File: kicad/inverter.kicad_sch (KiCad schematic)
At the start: 3 parts, among them Q2 2N3904

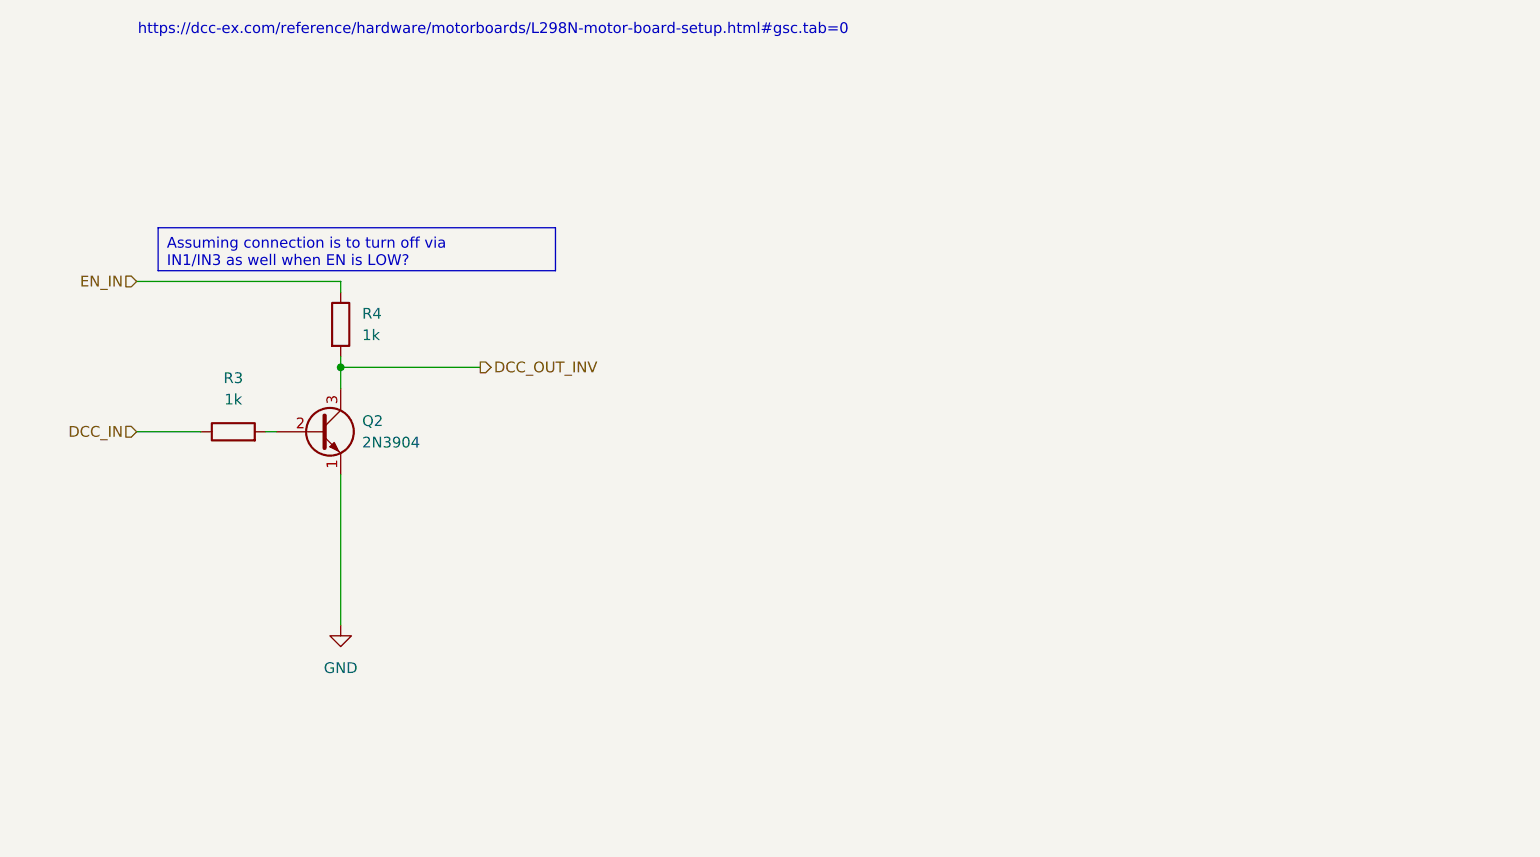
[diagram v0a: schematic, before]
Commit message: new screen, minimum functional
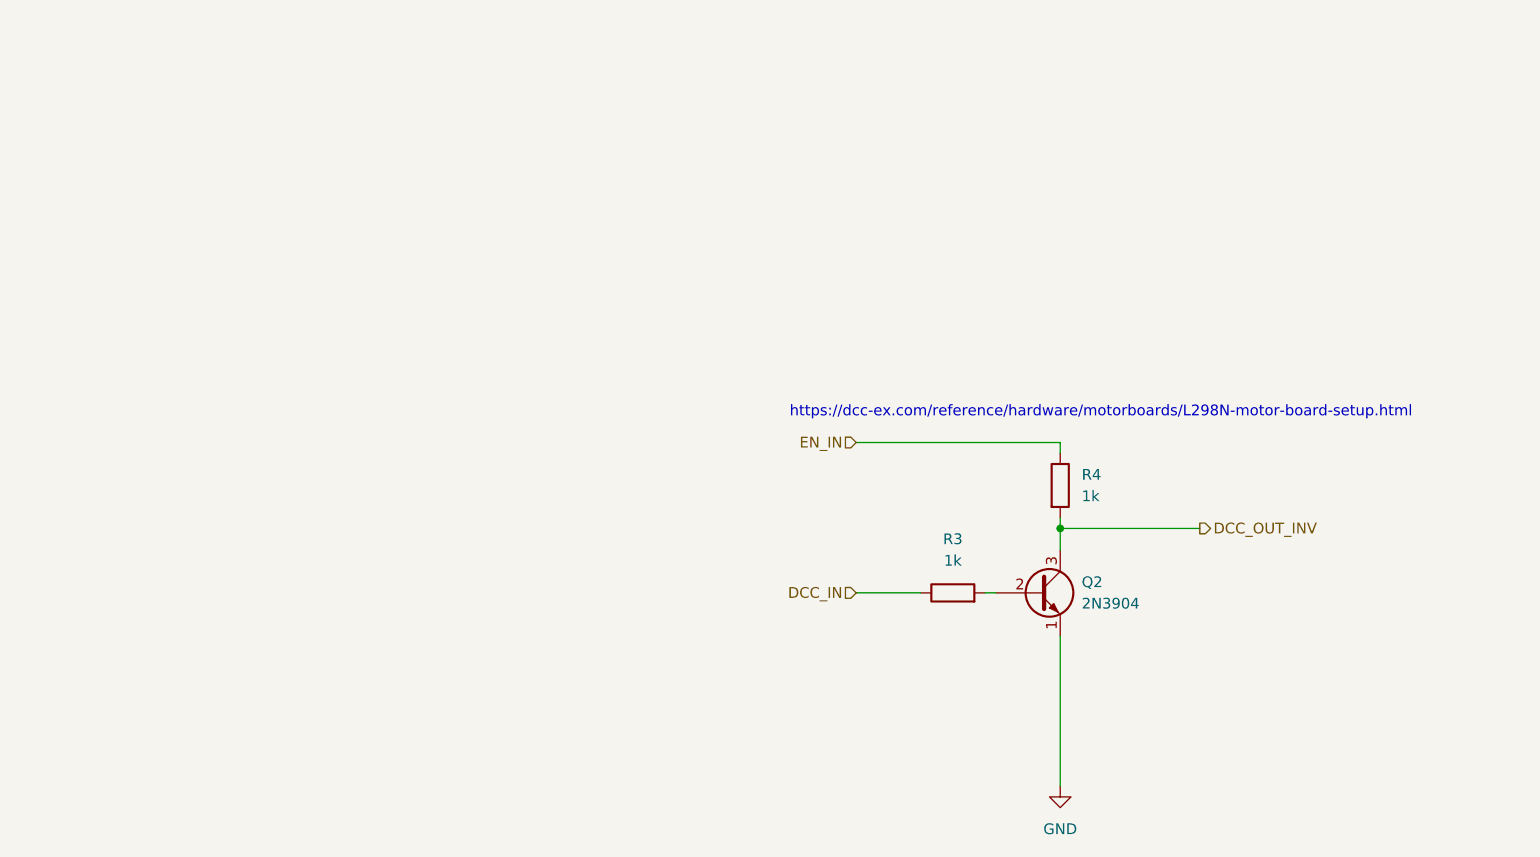
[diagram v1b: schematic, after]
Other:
- note added: "https://dcc-ex.com/reference/hardware/motorboards/L298N-motor-board-setup.html"
- note removed: "https://dcc-ex.com/reference/hardware/motorboards/L298N-motor-board-setup.html#gsc.tab=0"
- moved on the sheet: Q2, R3, R4
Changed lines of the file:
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@@
 	(paper "A4")
 	(junction
-		(at 55.88 85.09)
+		(at 140.97 104.14)
 		(diameter 0)
 		(color 0 0 0 0)
@@
 	(wire
 		(pts
-			(xy 55.88 85.09) (xy 55.88 87.63)
-		)
-		(stroke
-			(width 0.4064)
-			(type default)
-		)
-	)
-	(wire
-		(pts
-			(xy 31.75 92.71) (xy 39.37 92.71)
-		)
-		(stroke
-			(width 0.4064)
-			(type default)
-		)
-	)
-	(wire
-		(pts
-			(xy 46.99 92.71) (xy 48.26 92.71)
-		)
-		(stroke
-			(width 0.4064)
-			(type default)
-		)
-	)
-	(wire
-		(pts
-			(xy 55.88 83.82) (xy 55.88 85.09)
-		)
-		(stroke
-			(width 0.4064)
-			(type default)
-		)
-	)
-	(wire
-		(pts
-			(xy 55.88 74.93) (xy 55.88 76.2)
-		)
-		(stroke
-			(width 0.4064)
-			(type default)
-		)
-	)
-	(wire
-		(pts
-			(xy 31.75 74.93) (xy 55.88 74.93)
-		)
-		(stroke
-			(width 0.4064)
-			(type default)
-		)
-	)
-	(wire
-		(pts
-			(xy 55.88 85.09) (xy 72.39 85.09)
-		)
-		(stroke
-			(width 0.4064)
-			(type default)
-		)
-	)
-	(wire
-		(pts
-			(xy 55.88 97.79) (xy 55.88 115.57)
-		)
-		(stroke
-			(width 0.4064)
-			(type default)
-		)
-	)
-	(text_box "Assuming connection is to turn off via IN1/IN3 as well when EN is LOW?"
-		(exclude_from_sim no)
-		(at 34.29 68.58 0)
-		(size 46.99 5.08)
-		(stroke
-			(width 0)
-			(type default)
-		)
-		(fill
-			(type none)
-		)
+			(xy 140.97 104.14) (xy 140.97 106.68)
+		)
+		(stroke
+			(width 0.4064)
+			(type default)
+		)
+	)
+	(wire
+		(pts
+			(xy 116.84 111.76) (xy 124.46 111.76)
+		)
+		(stroke
+			(width 0.4064)
+			(type default)
+		)
+	)
+	(wire
+		(pts
+			(xy 132.08 111.76) (xy 133.35 111.76)
+		)
+		(stroke
+			(width 0.4064)
+			(type default)
+		)
+	)
+	(wire
+		(pts
+			(xy 140.97 102.87) (xy 140.97 104.14)
+		)
+		(stroke
+			(width 0.4064)
+			(type default)
+		)
+	)
+	(wire
+		(pts
+			(xy 140.97 93.98) (xy 140.97 95.25)
+		)
+		(stroke
+			(width 0.4064)
+			(type default)
+		)
+	)
+	(wire
+		(pts
+			(xy 116.84 93.98) (xy 140.97 93.98)
+		)
+		(stroke
+			(width 0.4064)
+			(type default)
+		)
+	)
+	(wire
+		(pts
+			(xy 140.97 104.14) (xy 157.48 104.14)
+		)
+		(stroke
+			(width 0.4064)
+			(type default)
+		)
+	)
+	(wire
+		(pts
+			(xy 140.97 116.84) (xy 140.97 134.62)
+		)
+		(stroke
+			(width 0.4064)
+			(type default)
+		)
+	)
+	(text "https://dcc-ex.com/reference/hardware/motorboards/L298N-motor-board-setup.html"
+		(exclude_from_sim no)
+		(at 145.796 90.424 0)
 		(effects
 			(font
 				(size 1.27 1.27)
 			)
-			(justify left top)
-		)
-	)
-	(text "https://dcc-ex.com/reference/hardware/motorboards/L298N-motor-board-setup.html#gsc.tab=0"
-		(exclude_from_sim no)
-		(at 73.914 45.212 0)
+			(href "https://dcc-ex.com/reference/hardware/motorboards/L298N-motor-board-setup.html")
+		)
+	)
+	(hierarchical_label "DCC_OUT_INV"
+		(shape output)
+		(at 157.48 104.14 0)
+		(fields_autoplaced yes)
 		(effects
 			(font
 				(size 1.27 1.27)
 			)
-		)
-	)
-	(hierarchical_label "DCC_OUT_INV"
-		(shape output)
-		(at 72.39 85.09 0)
+			(justify left)
+		)
+	)
+	(hierarchical_label "DCC_IN"
+		(shape input)
+		(at 116.84 111.76 180)
 		(fields_autoplaced yes)
 		(effects
@@
 				(size 1.27 1.27)
 			)
-			(justify left)
-		)
-	)
-	(hierarchical_label "DCC_IN"
+			(justify right)
+		)
+	)
+	(hierarchical_label "EN_IN"
 		(shape input)
-		(at 31.75 92.71 180)
+		(at 116.84 93.98 180)
 		(fields_autoplaced yes)
 		(effects
@@
 		)
 	)
-	(hierarchical_label "EN_IN"
-		(shape input)
-		(at 31.75 74.93 180)
-		(fields_autoplaced yes)
-		(effects
-			(font
-				(size 1.27 1.27)
-			)
-			(justify right)
-		)
-	)
 	(symbol
 		(lib_id "Device:R")
-		(at 43.18 92.71 90)
+		(at 128.27 111.76 90)
 		(unit 1)
 		(exclude_from_sim no)
@@
 		(fields_autoplaced yes)
 		(property "Reference" "R3"
-			(at 43.18 86.36 90)
+			(at 128.27 105.41 90)
 			(effects
 				(font
@@
 		)
 		(property "Value" "1k"
-			(at 43.18 88.9 90)
+			(at 128.27 107.95 90)
 			(effects
 				(font
@@
 		)
 		(property "Footprint" ""
-			(at 43.18 94.488 90)
+			(at 128.27 113.538 90)
 			(effects
 				(font
@@
 		)
 		(property "Datasheet" "~"
-			(at 43.18 92.71 0)
+			(at 128.27 111.76 0)
 			(effects
 				(font
@@
 		)
 		(property "Description" "Resistor"
-			(at 43.18 92.71 0)
+			(at 128.27 111.76 0)
 			(effects
 				(font
@@
 	(symbol
 		(lib_id "Transistor_BJT:2N3904")
-		(at 53.34 92.71 0)
+		(at 138.43 111.76 0)
 		(unit 1)
 		(exclude_from_sim no)
@@
 		(fields_autoplaced yes)
 		(property "Reference" "Q2"
-			(at 58.42 91.4399 0)
+			(at 143.51 110.4899 0)
 			(effects
 				(font
@@
 		)
 		(property "Value" "2N3904"
-			(at 58.42 93.9799 0)
+			(at 143.51 113.0299 0)
 			(effects
 				(font
@@
 		)
 		(property "Footprint" "Package_TO_SOT_THT:TO-92_Inline"
-			(at 58.42 94.615 0)
+			(at 143.51 113.665 0)
 			(effects
 				(font
@@
 		)
 		(property "Datasheet" "https://www.onsemi.com/pub/Collateral/2N3903-D.PDF"
-			(at 53.34 92.71 0)
+			(at 138.43 111.76 0)
 			(effects
 				(font
@@
 		)
 		(property "Description" "0.2A Ic, 40V Vce, Small Signal NPN Transistor, TO-92"
-			(at 53.34 92.71 0)
+			(at 138.43 111.76 0)
 			(effects
 				(font
@@
 	(symbol
 		(lib_id "Device:R")
-		(at 55.88 80.01 0)
+		(at 140.97 99.06 0)
 		(unit 1)
 		(exclude_from_sim no)
@@
 		(fields_autoplaced yes)
 		(property "Reference" "R4"
-			(at 58.42 78.7399 0)
+			(at 143.51 97.7899 0)
 			(effects
 				(font
@@
 		)
 		(property "Value" "1k"
-			(at 58.42 81.2799 0)
+			(at 143.51 100.3299 0)
 			(effects
 				(font
@@
 		)
 		(property "Footprint" ""
-			(at 54.102 80.01 90)
+			(at 139.192 99.06 90)
 			(effects
 				(font
@@
 		)
 		(property "Datasheet" "~"
-			(at 55.88 80.01 0)
+			(at 140.97 99.06 0)
 			(effects
 				(font
@@
 		)
 		(property "Description" "Resistor"
-			(at 55.88 80.01 0)
+			(at 140.97 99.06 0)
 			(effects
 				(font
@@
 	(symbol
 		(lib_id "power:GND")
-		(at 55.88 115.57 0)
+		(at 140.97 134.62 0)
 		(unit 1)
 		(exclude_from_sim no)
@@
 		(fields_autoplaced yes)
 		(property "Reference" "#PWR02"
-			(at 55.88 121.92 0)
+			(at 140.97 140.97 0)
 			(effects
 				(font
@@
 		)
 		(property "Value" "GND"
-			(at 55.88 120.65 0)
+			(at 140.97 139.7 0)
 			(effects
 				(font
@@
 		)
 		(property "Footprint" ""
-			(at 55.88 115.57 0)
+			(at 140.97 134.62 0)
 			(effects
 				(font
@@
 		)
 		(property "Datasheet" ""
-			(at 55.88 115.57 0)
+			(at 140.97 134.62 0)
 			(effects
 				(font
@@
 		)
 		(property "Description" "Power symbol creates a global label with name \"GND\" , ground"
-			(at 55.88 115.57 0)
-			(effects
-				(font
+			(at 140.97 134.62 0)
+			(effects
+				(font
